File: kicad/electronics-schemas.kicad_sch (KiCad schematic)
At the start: 0 parts

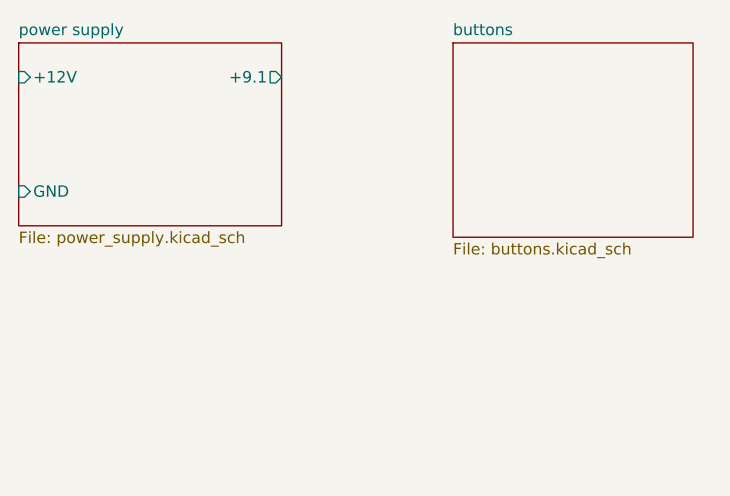
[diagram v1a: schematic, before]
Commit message: migliorato power supply schema aggiungendo zener e LM317 regolabile. aggiunto anche i calcoli.
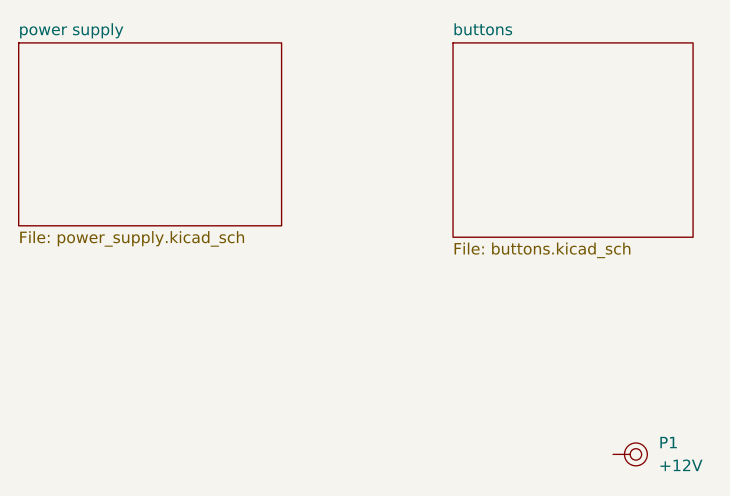
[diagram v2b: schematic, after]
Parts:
- added P1: +12V, dag-library:pad, symbol dag_library:pad
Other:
- sheet power supply ports: added none; removed +12V, +9.1, GND
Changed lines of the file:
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@@
 		(company "Dag-Electronics")
+	)
+	(symbol
+		(lib_id "dag_library:pad")
+		(at 93.98 67.31 0)
+		(unit 1)
+		(exclude_from_sim no)
+		(in_bom yes)
+		(on_board yes)
+		(dnp no)
+		(fields_autoplaced yes)
+		(property "Reference" "P1"
+			(at 99.06 66.0399 0)
+			(effects
+				(font
+					(size 1.27 1.27)
+				)
+				(justify left)
+			)
+		)
+		(property "Value" "+12V"
+			(at 99.06 68.5799 0)
+			(effects
+				(font
+					(size 1.27 1.27)
+				)
+				(justify left)
+			)
+		)
+		(property "Footprint" "dag-library:pad"
+			(at 94.488 72.39 0)
+			(effects
+				(font
+					(size 1.27 1.27)
+				)
+				(hide yes)
+			)
+		)
+		(property "Datasheet" ""
+			(at 93.98 67.31 0)
+			(effects
+				(font
+					(size 1.27 1.27)
+				)
+				(hide yes)
+			)
+		)
+		(property "Description" "Pad per saldature dirette sulla PCB"
+			(at 93.472 70.358 0)
+			(effects
+				(font
+					(size 1.27 1.27)
+				)
+				(hide yes)
+			)
+		)
+		(pin ""
+		)
+		(instances
+			(project ""
+				(path "/f1ade40e-ee4b-4e00-b57d-44850604005b"
+					(reference "P1")
+					(unit 1)
+				)
+			)
+		)
 	)
 	(sheet
@@
 			)
 		)
-		(pin "+9.1" output
-			(at 57.15 25.4 0)
-			(effects
-				(font
-					(size 1.27 1.27)
-				)
-				(justify right)
-			)
-		)
-		(pin "+12V" input
-			(at 27.94 25.4 180)
-			(effects
-				(font
-					(size 1.27 1.27)
-				)
-				(justify left)
-			)
-		)
-		(pin "GND" input
-			(at 27.94 38.1 180)
-			(effects
-				(font
-					(size 1.27 1.27)
-				)
-				(justify left)
-			)
-		)

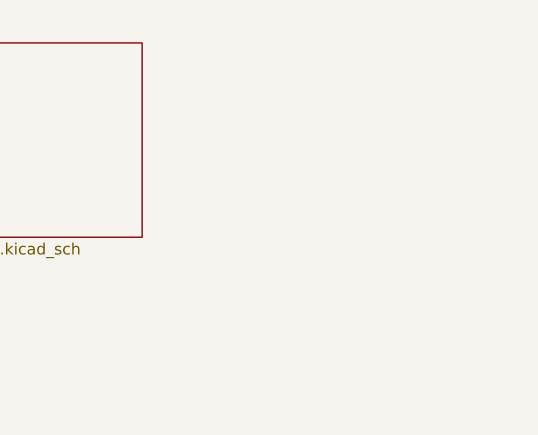
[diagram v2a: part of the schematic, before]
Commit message: aggiunto foglio per relay
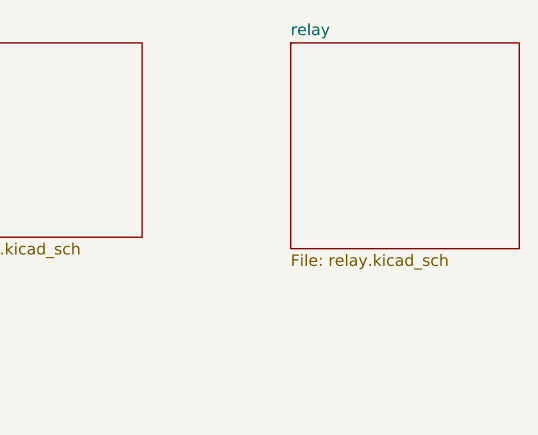
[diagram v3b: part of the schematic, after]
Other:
- added sheet relay (relay.kicad_sch)
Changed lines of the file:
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@@
 		(title "Main")
 		(date "2025-09-25")
-		(rev "v0.0.2")
+		(rev "v0.0.3")
 		(company "Dag-Electronics")
 	)
@@
 				)
 			)
+		)
+	)
+	(sheet
+		(at 119.38 21.59)
+		(size 25.4 22.86)
+		(exclude_from_sim no)
+		(in_bom yes)
+		(on_board yes)
+		(dnp no)
+		(fields_autoplaced yes)
+		(stroke
+			(width 0.1524)
+			(type solid)
+		)
+		(fill
+			(color 0 0 0 0.0000)
+		)
+		(property "Sheetname" "relay"
+			(at 119.38 20.8784 0)
+			(effects
+				(font
+					(size 1.27 1.27)
+				)
+				(justify left bottom)
+			)
+		)
+		(property "Sheetfile" "relay.kicad_sch"
+			(at 119.38 45.0346 0)
+			(effects
+				(font
+					(size 1.27 1.27)
+				)
+				(justify left top)
+			)
+		)
+		(instances
+			(project "electronics-schemas"
+				(path "/f1ade40e-ee4b-4e00-b57d-44850604005b"
+					(page "4")
+				)
+			)

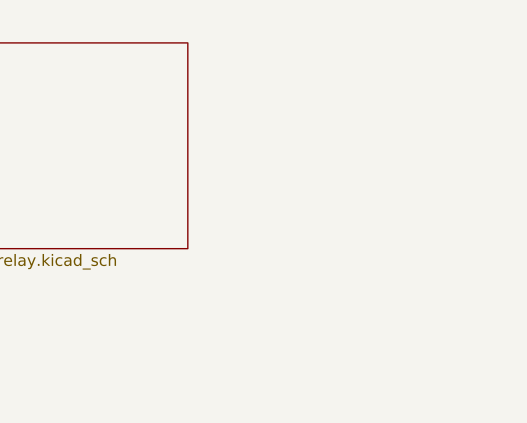
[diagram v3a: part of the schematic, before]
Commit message: Aggiunto foglio LCD con bus e etichette
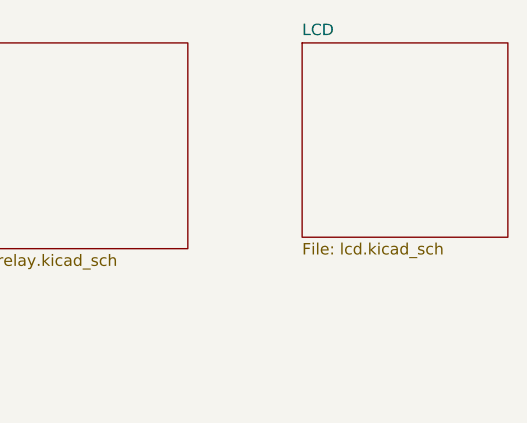
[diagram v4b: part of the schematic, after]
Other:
- added sheet LCD (lcd.kicad_sch)
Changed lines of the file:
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@@
+	)
+	(sheet
+		(at 157.48 21.59)
+		(size 22.86 21.59)
+		(exclude_from_sim no)
+		(in_bom yes)
+		(on_board yes)
+		(dnp no)
+		(fields_autoplaced yes)
+		(stroke
+			(width 0.1524)
+			(type solid)
+		)
+		(fill
+			(color 0 0 0 0.0000)
+		)
+		(property "Sheetname" "LCD"
+			(at 157.48 20.8784 0)
+			(effects
+				(font
+					(size 1.27 1.27)
+				)
+				(justify left bottom)
+			)
+		)
+		(property "Sheetfile" "lcd.kicad_sch"
+			(at 157.48 43.7646 0)
+			(effects
+				(font
+					(size 1.27 1.27)
+				)
+				(justify left top)
+			)
+		)
+		(instances
+			(project "electronics-schemas"
+				(path "/f1ade40e-ee4b-4e00-b57d-44850604005b"
+					(page "5")
+				)
+			)
+		)
 	)
 	(sheet

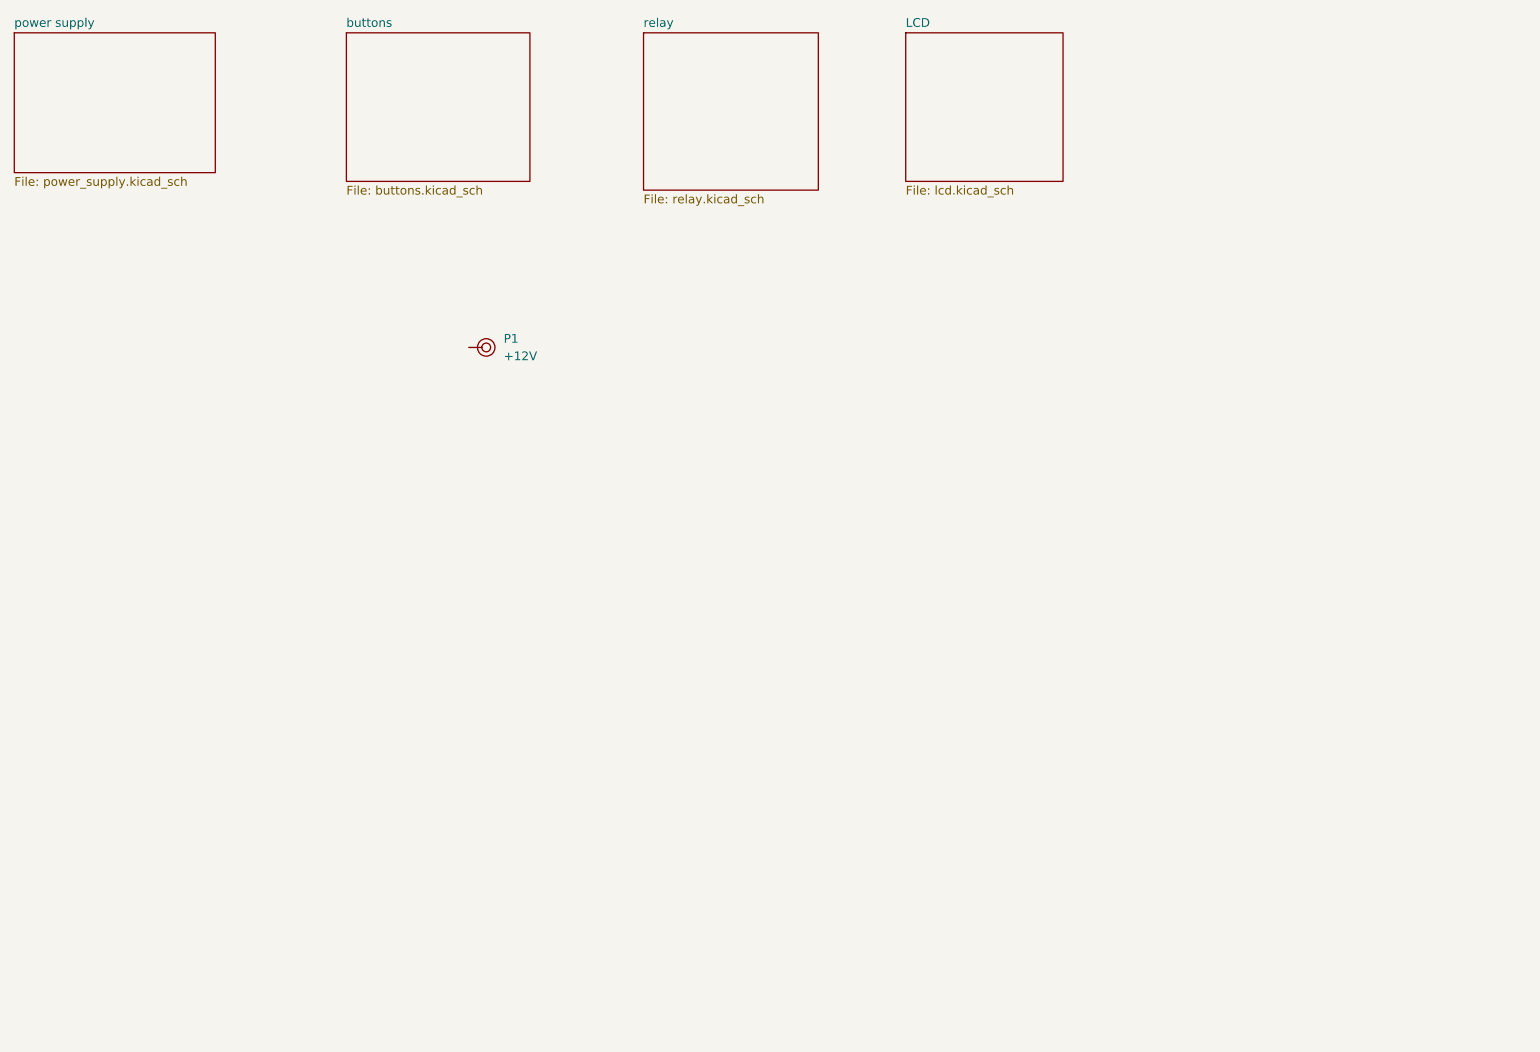
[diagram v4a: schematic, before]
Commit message: esempio di relay su circuito
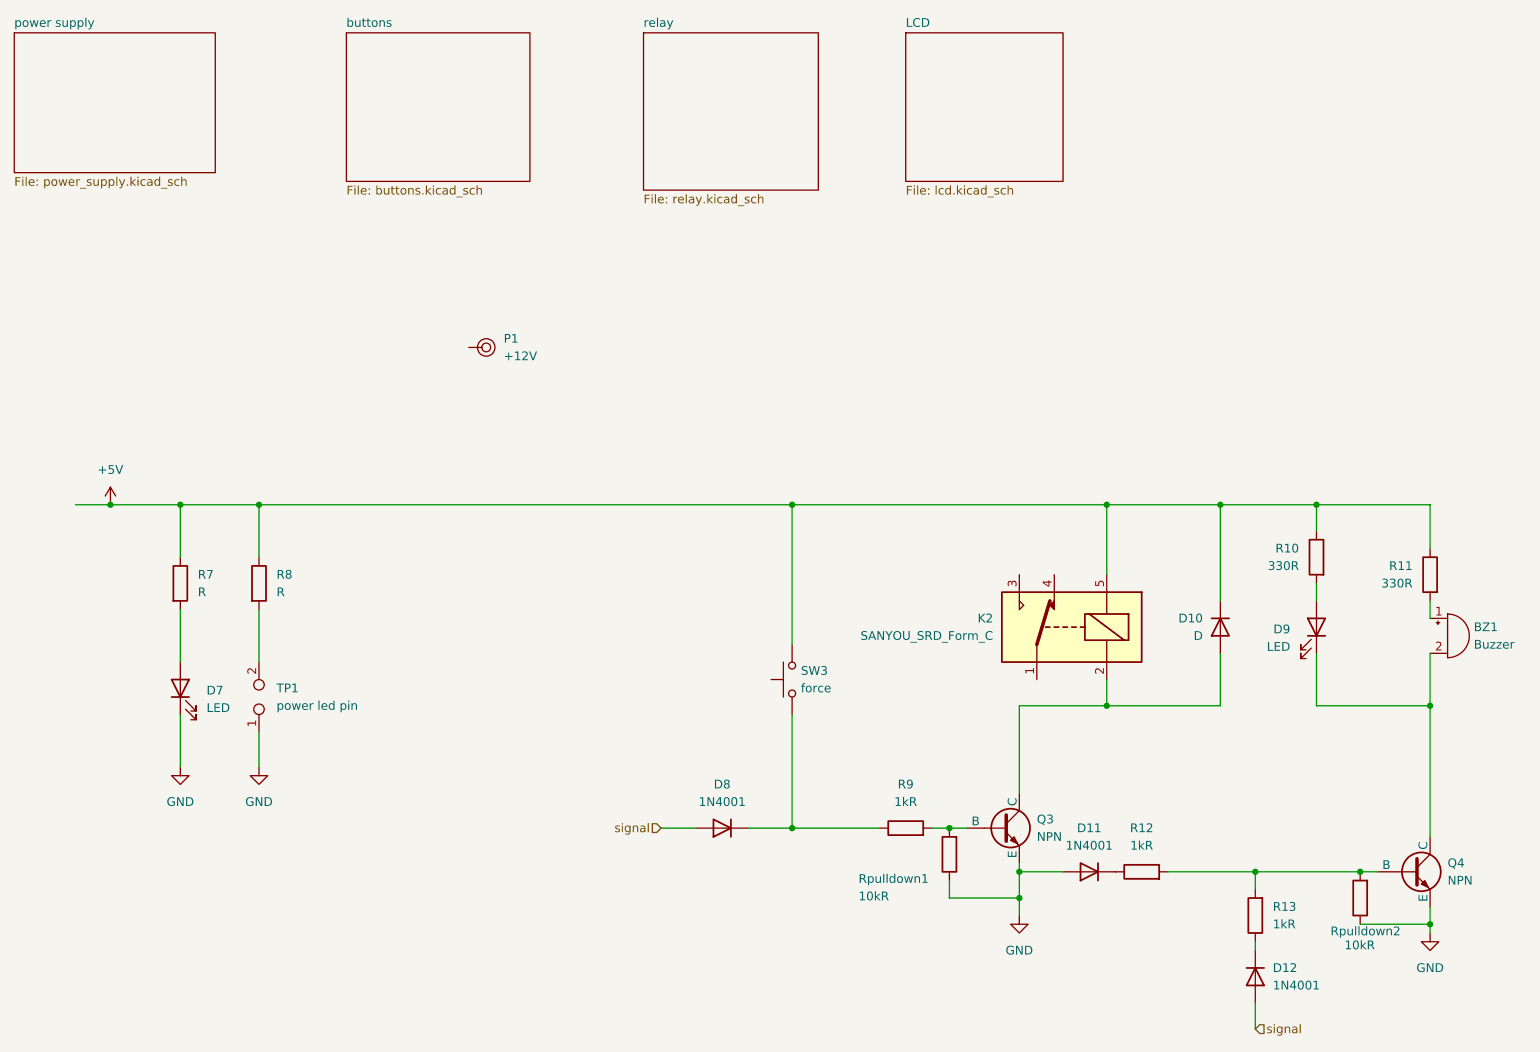
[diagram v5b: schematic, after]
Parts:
- added BZ1: Buzzer, symbol Device:Buzzer
- added D10: D, symbol Device:D
- added D11, D12, D8: 1N4001, Diode_THT:D_DO-41_SOD81_P10.16mm_Horizontal, symbol Diode:1N4001
- added D7, D9: LED, symbol Device:LED
- added K2: SANYOU_SRD_Form_C, Relay_THT:Relay_SPDT_SANYOU_SRD_Series_Form_C, symbol Relay:SANYOU_SRD_Form_C
- added Q3, Q4: NPN, symbol Simulation_SPICE:NPN
- added R10, R11: 330R, symbol Device:R
- added R12, R13, R9: 1kR, symbol Device:R
- added R7, R8: R, symbol Device:R
- added Rpulldown1, Rpulldown2: 10kR, symbol Device:R
- added SW3: force, symbol Switch:SW_Push
- added TP1: power led pin, Connector_PinSocket_2.54mm:PinSocket_1x02_P2.54mm_Vertical_SMD_Pin1Left, symbol Connector:TestPoint_2Pole
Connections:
- new net: D7.2 (A), R7.2
- new net: D12.1 (K), R13.1
- new net: Q4.2 (B), R12.2, R13.2, Rpulldown2.2
- new net: D10.2 (A), K2.2, Q3.1 (C)
- new net: D9.2 (A), R10.2
- new net: BZ1.1 (+), R11.2
- new net: BZ1.2 (-), D9.1 (K), Q4.1 (C)
- new net: Q3.2 (B), R9.2, Rpulldown1.2
- new net: R8.2, TP1.2
- new net: D8.1 (K), R9.1, SW3.1
- new net: D11.1 (K), R12.1
- new net +5V: D10.1 (K), K2.5, R10.1, R11.1, R7.1, R8.1, SW3.2
- new net GND: D11.2 (A), D7.1 (K), Q3.3 (E), Q4.3 (E), Rpulldown1.1, Rpulldown2.1, TP1.1
- new net signal: D12.2 (A), D8.2 (A)

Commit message: aggiustato il segnale comiune
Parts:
- removed R12: 1kR, symbol Device:R
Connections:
- net GND: no longer D11.2 (A)
- net at R13.1: now also Q4.2 (B), Rpulldown2.2; no longer D12.1 (K)
- net at D8.1 (K), R9.1, SW3.1: now also D11.2 (A)
- net at D11.1 (K): now also D12.1 (K), R13.2
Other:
- moved on the sheet: BZ1, D10, D12, D7, D8, D9, K2, Q3, Q4, R10, R11, R13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

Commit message: bug fixed
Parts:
- removed BZ1: Buzzer, symbol Device:Buzzer
- removed D10: D, symbol Device:D
- removed D11, D12, D8: 1N4001, Diode_THT:D_DO-41_SOD81_P10.16mm_Horizontal, symbol Diode:1N4001
- removed D7, D9: LED, symbol Device:LED
- removed K2: SANYOU_SRD_Form_C, Relay_THT:Relay_SPDT_SANYOU_SRD_Series_Form_C, symbol Relay:SANYOU_SRD_Form_C
- removed Q3, Q4: NPN, symbol Simulation_SPICE:NPN
- removed R10, R11: 330R, symbol Device:R
- removed R13, R9: 1kR, symbol Device:R
- removed R7, R8: R, symbol Device:R
- removed Rpulldown1, Rpulldown2: 10kR, symbol Device:R
- removed SW3: force, symbol Switch:SW_Push
- removed TP1: power led pin, Connector_PinSocket_2.54mm:PinSocket_1x02_P2.54mm_Vertical_SMD_Pin1Left, symbol Connector:TestPoint_2Pole
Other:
- added sheet Untitled Sheet (untitled.kicad_sch)

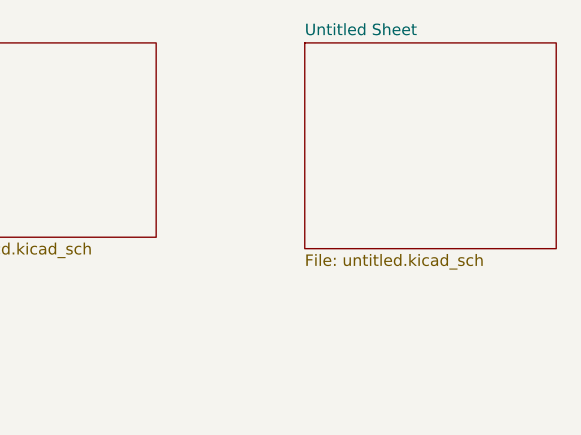
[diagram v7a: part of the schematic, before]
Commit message: aggiunto schema per motori PWM
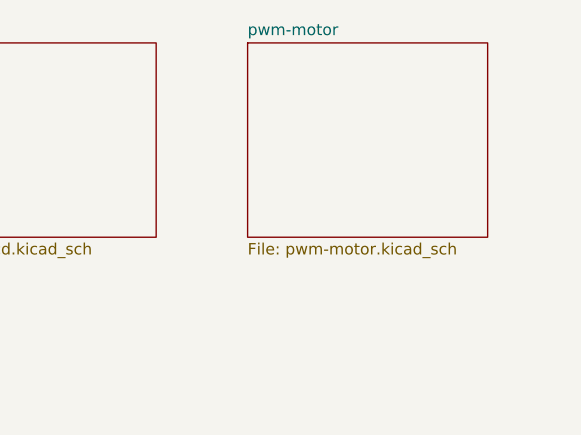
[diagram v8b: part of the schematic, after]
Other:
- removed sheet Untitled Sheet
- added sheet pwm-motor (pwm-motor.kicad_sch)
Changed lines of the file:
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@@
 		(company "Dag-Electronics")
+	)
+	(bus_alias "LCD"
+		(members "LCD.GND" "LCD.Vcc" "LCD.SDA" "LCD.SCL")
 	)
 	(symbol
@@
 	)
 	(sheet
-		(at 196.85 21.59)
-		(size 27.94 22.86)
-		(exclude_from_sim no)
-		(in_bom yes)
-		(on_board yes)
-		(dnp no)
-		(fields_autoplaced yes)
-		(stroke
-			(width 0.1524)
-			(type solid)
-		)
-		(fill
-			(color 0 0 0 0.0000)
-		)
-		(property "Sheetname" "Untitled Sheet"
-			(at 196.85 20.8784 0)
-			(effects
-				(font
-					(size 1.27 1.27)
-				)
-				(justify left bottom)
-			)
-		)
-		(property "Sheetfile" "untitled.kicad_sch"
-			(at 196.85 45.0346 0)
-			(effects
-				(font
+		(at 190.5 21.59)
+		(size 26.67 21.59)
+		(exclude_from_sim no)
+		(in_bom yes)
+		(on_board yes)
+		(dnp no)
+		(fields_autoplaced yes)
+		(stroke
+			(width 0.1524)
+			(type solid)
+		)
+		(fill
+			(color 0 0 0 0.0000)
+		)
+		(property "Sheetname" "pwm-motor"
+			(at 190.5 20.8784 0)
+			(effects
+				(font
+					(size 1.27 1.27)
+				)
+				(justify left bottom)
+			)
+		)
+		(property "Sheetfile" "pwm-motor.kicad_sch"
+			(at 190.5 43.7646 0)
+			(effects
+				(font
